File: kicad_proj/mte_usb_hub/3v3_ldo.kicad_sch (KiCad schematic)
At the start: 6 parts

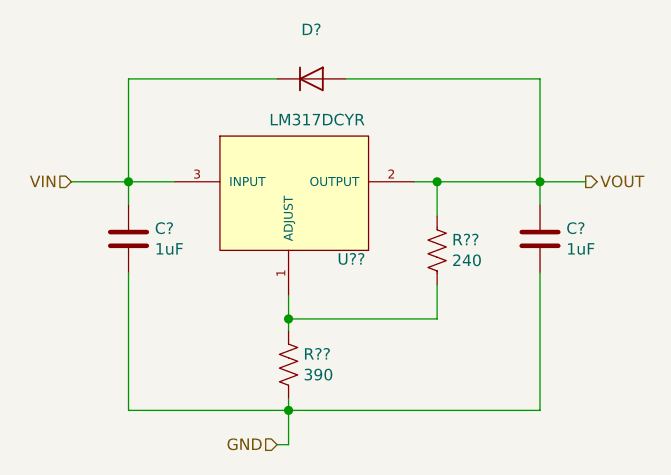
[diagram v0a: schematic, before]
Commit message: Updates input protection, output BC enabled
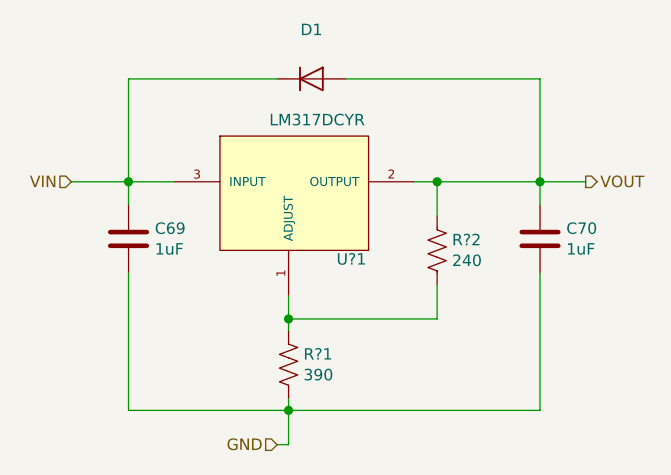
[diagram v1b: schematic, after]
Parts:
- gave numbers to parts that had none: 6
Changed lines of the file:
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@@
-(kicad_sch (version 20210126) (generator eeschema)
+(kicad_sch (version 20210406) (generator eeschema)
   (paper "A4")
   (junction (at 35.56 33.02) (diameter 1.016) (color 0 0 0 0))
@@
   (symbol (lib_id "mte_usb_hub:RC0402FR-07390RL") (at 53.34 53.34 0) (unit 1)
     (in_bom yes) (on_board yes)
-    (property "Reference" "R??" (id 0) (at 54.9911 52.1906 0)
+    (property "Reference" "R?1" (id 0) (at 54.9911 52.1906 0)
       (effects (font (size 1.27 1.27)) (justify left))
     )
@@
   (symbol (lib_id "mte_usb_hub:RC0402JR-07240RL") (at 69.85 40.64 0) (unit 1)
     (in_bom yes) (on_board yes)
-    (property "Reference" "R??" (id 0) (at 71.5011 39.4906 0)
+    (property "Reference" "R?2" (id 0) (at 71.5011 39.4906 0)
       (effects (font (size 1.27 1.27)) (justify left))
     )
@@
   (symbol (lib_id "diodes:BAS16GWJ") (at 55.88 21.59 0) (unit 1)
     (in_bom yes) (on_board yes)
-    (property "Reference" "D?" (id 0) (at 55.88 16.1352 0))
+    (property "Reference" "D1" (id 0) (at 55.88 16.1352 0))
     (property "Value" "BAS16GWJ" (id 1) (at 55.88 24.13 0)
       (effects (font (size 1.27 1.27)) hide)
@@
   (symbol (lib_id "mte_usb_hub:CC0402KRX5R7BB105") (at 35.56 39.37 0) (unit 1)
     (in_bom yes) (on_board yes)
-    (property "Reference" "C?" (id 0) (at 38.4811 38.2206 0)
+    (property "Reference" "C69" (id 0) (at 38.4811 38.2206 0)
       (effects (font (size 1.27 1.27)) (justify left))
     )
@@
   (symbol (lib_id "mte_usb_hub:CC0402KRX5R7BB105") (at 81.28 39.37 0) (unit 1)
     (in_bom yes) (on_board yes)
-    (property "Reference" "C?" (id 0) (at 84.2011 38.2206 0)
+    (property "Reference" "C70" (id 0) (at 84.2011 38.2206 0)
       (effects (font (size 1.27 1.27)) (justify left))
     )
@@
   (symbol (lib_id "mte_usb_hub:LM317DCYR") (at 53.34 33.02 0) (unit 1)
     (in_bom yes) (on_board yes)
-    (property "Reference" "U??" (id 0) (at 60.325 41.6368 0))
+    (property "Reference" "U?1" (id 0) (at 60.325 41.6368 0))
     (property "Value" "LM317DCYR" (id 1) (at 60.96 41.91 0)
       (effects (font (size 1.27 1.27)) hide)

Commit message: New changes from the livestream
Starts the layout
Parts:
- C69, C70: footprint footprints:CAPACITOR_0402N -> mte_usb_footprints:CAPACITOR_0402N
- D1: footprint footprints:SODFL360X160X130L45X62N -> mte_usb_footprints:SODFL360X160X130L45X62N
- R?1, R?2: footprint footprints:RESISTOR_0402N -> mte_usb_footprints:RESISTOR_0402N
- U?1: footprint footprints:SOT223-4P230_700X180L80X75N -> mte_usb_footprints:SOT223-4P230_700X180L80X75N
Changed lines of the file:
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@@
       (effects (font (size 1.27 1.27)) hide)
     )
-    (property "Footprint" "footprints:RESISTOR_0402N" (id 2) (at 54.356 53.594 90)
+    (property "Footprint" "mte_usb_footprints:RESISTOR_0402N" (id 2) (at 54.356 53.594 90)
       (effects (font (size 1.27 1.27)) hide)
     )
@@
       (effects (font (size 1.27 1.27)) hide)
     )
-    (property "Footprint" "footprints:RESISTOR_0402N" (id 2) (at 70.866 40.894 90)
+    (property "Footprint" "mte_usb_footprints:RESISTOR_0402N" (id 2) (at 70.866 40.894 90)
       (effects (font (size 1.27 1.27)) hide)
     )
@@
       (effects (font (size 1.27 1.27)) hide)
     )
-    (property "Footprint" "footprints:SODFL360X160X130L45X62N" (id 2) (at 55.88 21.59 0)
+    (property "Footprint" "mte_usb_footprints:SODFL360X160X130L45X62N" (id 2) (at 55.88 21.59 0)
       (effects (font (size 1.27 1.27)) hide)
     )
@@
       (effects (font (size 1.27 1.27)) (justify left) hide)
     )
-    (property "Footprint" "footprints:CAPACITOR_0402N" (id 2) (at 36.5252 43.18 0)
+    (property "Footprint" "mte_usb_footprints:CAPACITOR_0402N" (id 2) (at 36.5252 43.18 0)
       (effects (font (size 1.27 1.27)) hide)
     )
@@
       (effects (font (size 1.27 1.27)) (justify left) hide)
     )
-    (property "Footprint" "footprints:CAPACITOR_0402N" (id 2) (at 82.2452 43.18 0)
+    (property "Footprint" "mte_usb_footprints:CAPACITOR_0402N" (id 2) (at 82.2452 43.18 0)
       (effects (font (size 1.27 1.27)) hide)
     )
@@
       (effects (font (size 1.27 1.27)) hide)
     )
-    (property "Footprint" "footprints:SOT223-4P230_700X180L80X75N" (id 2) (at 53.34 33.02 0)
+    (property "Footprint" "mte_usb_footprints:SOT223-4P230_700X180L80X75N" (id 2) (at 53.34 33.02 0)
       (effects (font (size 1.27 1.27)) hide)
     )
